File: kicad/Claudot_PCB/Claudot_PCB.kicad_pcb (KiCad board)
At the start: 2 copper layers, 104.8 x 57.2 mm, 51 parts, among them SW1 SW_Push, SW10 SW_Push, SW11 SW_Push, SW12 RotaryEncoder, SW2 SW_Push, SW3 SW_Push, SW4 SW_Push, SW5 SW_Push, SW6 SW_Push, SW7 SW_Push, SW8 SW_Push, SW9 SW_Push, U1 RP2040, U2 AP2112K-3.3, U3 W25Q16JVUXIQ, Y1 12MHz

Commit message: Update schematic and pcb
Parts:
- added R5: 27, Library:R_0402, F.Cu at (121.3, 88.2)
- added R6: 27, Library:R_0402, F.Cu at (122.3, 88.2)
- moved C4 3.58 mm to (124.3, 89.5), turned to 0 degrees
- moved C3 2.58 mm to (124.3, 90.5), turned to 0 degrees
- moved C10 1.05 mm to (124.3, 91.5)
- moved C6 0.60 mm to (113.8, 96.5)
- moved C8 0.60 mm to (124.3, 96.5)
- moved C11 0.25 mm to (120.3, 88.2)
- moved C12 0.25 mm to (119.3, 88.2)
- moved C14 0.25 mm to (118.3, 88.2)
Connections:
- U1 pad 46: unconnected-(U1-USB_DM-Pad46) -> D-
- U1 pad 47: unconnected-(U1-USB_DP-Pad47) -> D+
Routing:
- net GND: vias 10 -> 11
- net +1V1: vias 0 -> 2

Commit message: Update schematic and pcb
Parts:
- added J1: Conn_01x04, Connector_Molex:Molex_Pico-EZmate_78171-0004_1x04-1MP_P1.20mm_Vertical, F.Cu at (120.2, 82.5)
- added R3: 10K, Resistor_SMD:R_0402_1005Metric, F.Cu at (109.2, 88.3)
- added R4: 1K, Resistor_SMD:R_0402_1005Metric, F.Cu at (109.2, 89.3)
- moved C15 3.95 mm to (114.8, 83.0), turned to 180 degrees
- moved C16 3.51 mm to (114.8, 87.7), turned to 180 degrees
- moved C4 3.28 mm to (121.1, 90.0), turned to 90 degrees
- moved R6 3.02 mm to (119.8, 86.5)
- moved C3 2.27 mm to (122.1, 90.0), turned to 90 degrees
- moved U3 2.15 mm to (114.3, 85.3), turned to 180 degrees
- moved C10 1.88 mm to (123.1, 90.0), turned to 90 degrees
- moved R5 1.77 mm to (120.8, 86.5)
- moved C11 0.82 mm to (119.5, 88.4)
- moved C12 0.82 mm to (118.5, 88.4)
- moved C14 0.82 mm to (117.5, 88.4)
- moved U2 0.80 mm to (114.3, 89.5)
- renumbered U3 to U2, U2 to U3
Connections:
- net Net-(U1-QSPI_SS) renamed QSPI_SS_N
- net Net-(U1-RUN) renamed ~{RESET}
- C16 pad 1: Net-(U2-VOUT) -> +3V3
- R5 pad 1: D+ -> Net-(U1-USB_DM)
- R5 pad 2: unconnected-(R5-Pad2) -> D-
- R6 pad 1: D- -> Net-(U1-USB_DP)
- R6 pad 2: unconnected-(R6-Pad2) -> D+
- U1 pad 46: D- -> Net-(U1-USB_DM)
- U1 pad 47: D+ -> Net-(U1-USB_DP)
- U3 pad 5: Net-(U2-VOUT) -> +3V3
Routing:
- net GND: vias 11 -> 18
- net +3V3: vias 0 -> 4
- net +1V1: vias 2 -> 0

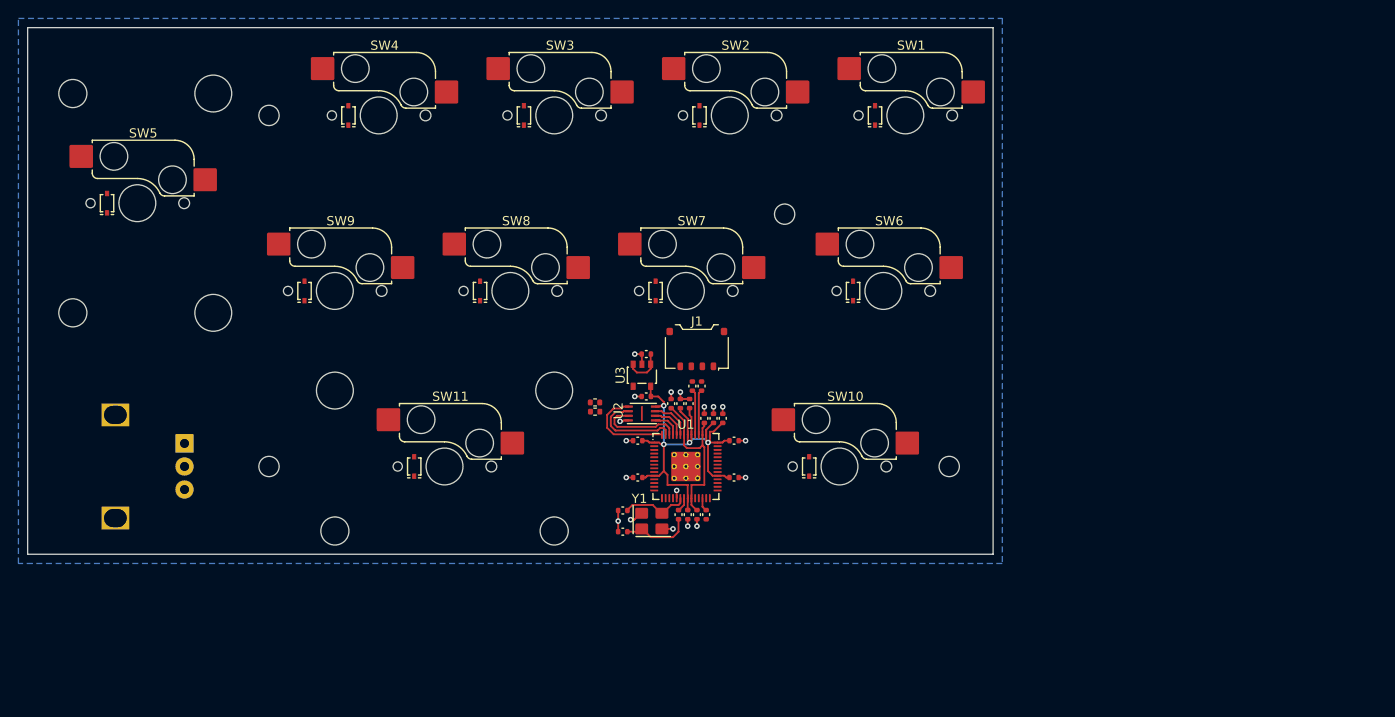
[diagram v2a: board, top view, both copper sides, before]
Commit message: Change J1 footprint
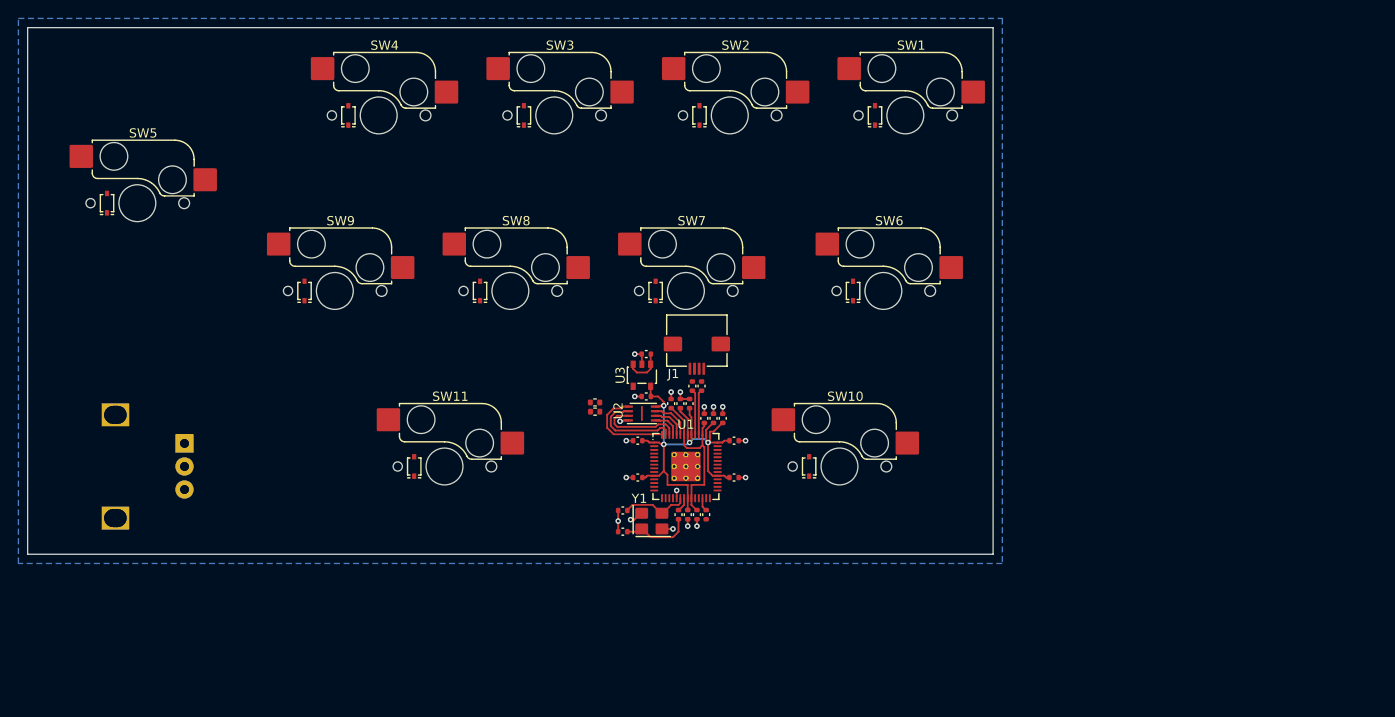
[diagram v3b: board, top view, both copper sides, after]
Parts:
- removed REF** (x2): MX_Switch_Stabilizer_2u, Library:MX_Switch_Stabilizer_2u
- removed REF** (x4): MountingHole_2.2mm_M2, MountingHole:MountingHole_2.2mm_M2
- J1: footprint Connector_Molex:Molex_Pico-EZmate_78171-0004_1x04-1MP_P1.20mm_Vertical -> Library:AFC01-S04FCC-00
- moved J1 0.80 mm to (120.2, 83.3)

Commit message: Update
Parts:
- added SW_B1: SKRP_Switch, Library:SKRP_Switch, F.Cu at (109.6, 114.1)
- added SW_R1: SKRP_Switch, Library:SKRP_Switch, F.Cu at (109.6, 118.7)
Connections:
- net QSPI_SS_N renamed QSPI_SS
- R4 pad 2: unconnected-(R4-Pad2) -> Net-(R4-Pad2)

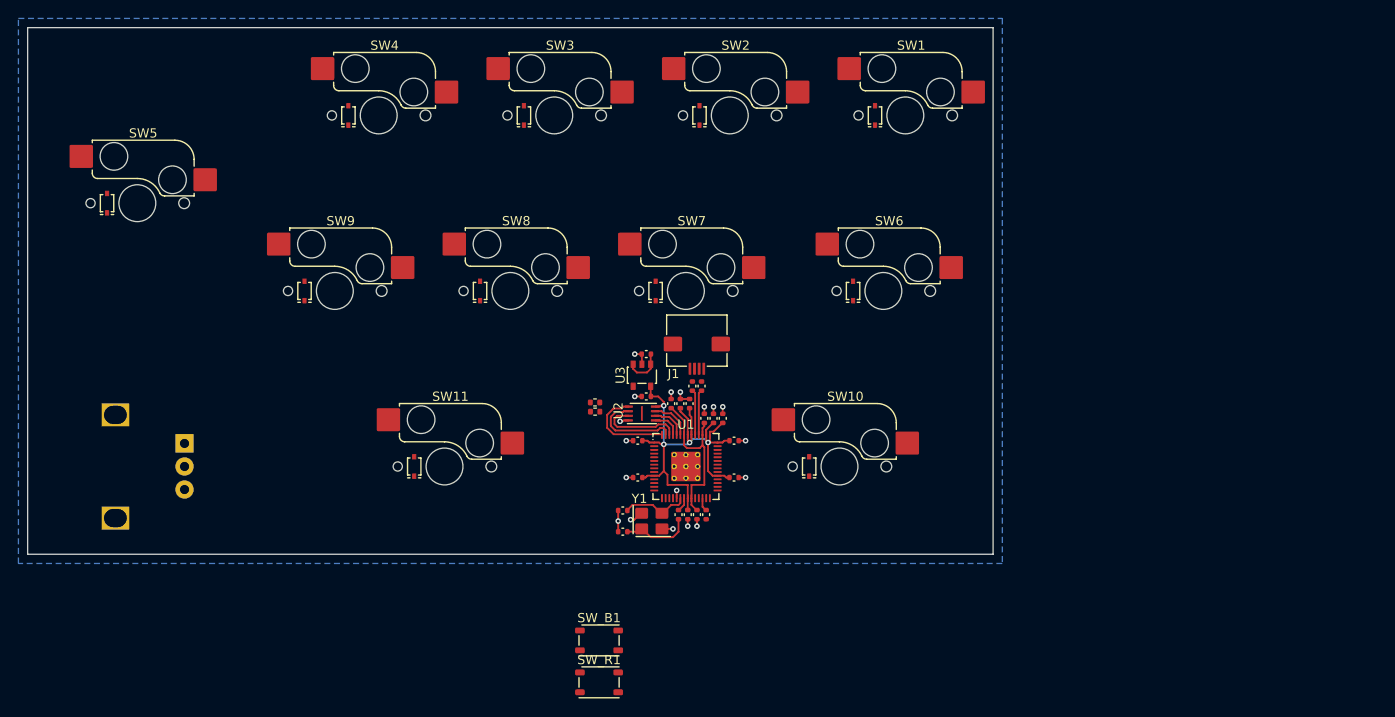
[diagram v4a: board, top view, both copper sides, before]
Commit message: Fix: restore missing hole
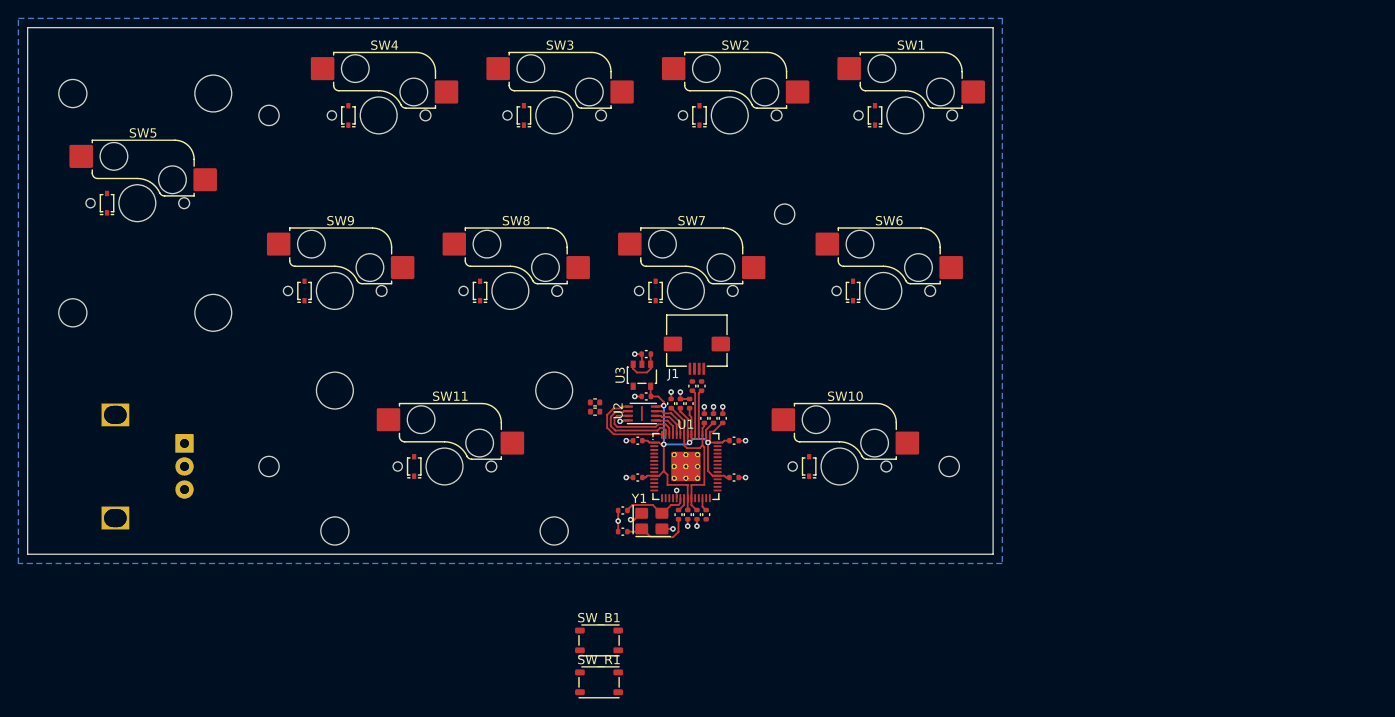
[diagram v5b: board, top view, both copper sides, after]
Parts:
- added REF**: MountingHole_2.2mm_M2, MountingHole:MountingHole_2.2mm_M2, B.Cu at (73.8, 95.2)
- added REF**: MountingHole_2.2mm_M2, MountingHole:MountingHole_2.2mm_M2, B.Cu at (129.8, 67.9)
- added REF**: MountingHole_2.2mm_M2, MountingHole:MountingHole_2.2mm_M2, B.Cu at (73.8, 57.1)
- added REF**: MX_Switch_Stabilizer_2u, Library:MX_Switch_Stabilizer_2u, B.Cu at (59.5, 66.7)
- added REF**: MountingHole_2.2mm_M2, MountingHole:MountingHole_2.2mm_M2, B.Cu at (147.6, 95.2)
- added REF**: MX_Switch_Stabilizer_2u, Library:MX_Switch_Stabilizer_2u, B.Cu at (92.9, 95.2)

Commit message: Update schematic and pcb
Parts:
- moved SW_R1 22.0 mm to (104.8, 97.2)
- moved SW_B1 21.4 mm to (104.8, 93.2)
- moved J1 0.09 mm to (120.3, 83.4)
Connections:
- R4 pad 1: QSPI_SS -> Net-(R4-Pad1)
- R4 pad 2: Net-(R4-Pad2) -> QSPI_SS
- SW_B1 pad 1: GND -> Net-(R4-Pad1)
- SW_B1 pad 2: (no net) -> Net-(R4-Pad1)
- SW_B1 pad 3: Net-(R4-Pad2) -> GND
- SW_B1 pad 4: (no net) -> GND
- SW_R1 pad 1: GND -> ~{RESET}
- SW_R1 pad 2: (no net) -> ~{RESET}
- SW_R1 pad 3: ~{RESET} -> GND
- SW_R1 pad 4: (no net) -> GND
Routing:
- net GND: vias 18 -> 19
- net +5V: vias 0 -> 2
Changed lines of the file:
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@@
 	(net 87 "~{RESET}")
 	(net 88 "QSPI_SS")
-	(net 89 "Net-(R4-Pad2)")
+	(net 89 "Net-(R4-Pad1)")
 	(footprint "Library:AFC01-S04FCC-00"
 		(layer "F.Cu")
-		(at 120.25 83.3 180)
+		(at 120.2625 83.385 180)
 		(tags "JUSHUO, FFC")
 		(property "Reference" "J1"
@@
 	(footprint "Library:SKRP_Switch"
 		(layer "F.Cu")
-		(at 109.6375 118.675)
+		(at 104.76875 97.25)
 		(tags "ALPSALPINE, SKRPABE010, C115360")
 		(property "Reference" "SW_R1"
@@
 		)
 		(property "Value" "SKRP_Switch"
-			(at 0 0 0)
+			(at 0 2.5 0)
 			(unlocked yes)
 			(layer "F.Fab")
+			(hide yes)
 			(effects
 				(font
-					(size 0.5 0.5)
-					(thickness 0.075)
+					(size 1 1)
+					(thickness 0.15)
 				)
 			)
@@
 		)
 		(fp_text user "${REFERENCE}"
-			(at 0 2.5 0)
+			(at 0 0 0)
 			(unlocked yes)
 			(layer "F.Fab")
 			(effects
 				(font
-					(size 1 1)
-					(thickness 0.15)
+					(size 0.5 0.5)
+					(thickness 0.075)
 				)
 			)
@@
 			(layers "F.Cu" "F.Mask" "F.Paste")
 			(roundrect_rratio 0.2307692308)
-			(net 46 "GND")
+			(net 87 "~{RESET}")
 			(pinfunction "1")
 			(pintype "passive")
@@
 			(layers "F.Cu" "F.Mask" "F.Paste")
 			(roundrect_rratio 0.2307692308)
+			(net 87 "~{RESET}")
+			(pinfunction "2")
+			(pintype "passive")
 			(thermal_bridge_angle 45)
 		)
@@
 			(layers "F.Cu" "F.Mask" "F.Paste")
 			(roundrect_rratio 0.2307692308)
-			(net 87 "~{RESET}")
+			(net 46 "GND")
 			(pinfunction "3")
 			(pintype "passive")
@@
 			(layers "F.Cu" "F.Mask" "F.Paste")
 			(roundrect_rratio 0.2307692308)
+			(net 46 "GND")
+			(pinfunction "4")
+			(pintype "passive")
 			(thermal_bridge_angle 45)
 		)
@@
 			(layers "F.Cu" "F.Mask" "F.Paste")
 			(roundrect_rratio 0.25)
-			(net 88 "QSPI_SS")
+			(net 89 "Net-(R4-Pad1)")
 			(pintype "passive")
 		)
@@
 			(layers "F.Cu" "F.Mask" "F.Paste")
 			(roundrect_rratio 0.25)
-			(net 89 "Net-(R4-Pad2)")
+			(net 88 "QSPI_SS")
 			(pintype "passive")
 		)
@@
 	(footprint "Library:SKRP_Switch"
 		(layer "F.Cu")
-		(at 109.6375 114.125)
+		(at 104.76875 93.25)
 		(tags "ALPSALPINE, SKRPABE010, C115360")
 		(property "Reference" "SW_B1"
@@
 		)
 		(property "Value" "SKRP_Switch"
-			(at 0 0 0)
+			(at 0 2.5 0)
 			(unlocked yes)
 			(layer "F.Fab")
+			(hide yes)
 			(effects
 				(font
-					(size 0.5 0.5)
-					(thickness 0.075)
+					(size 1 1)
+					(thickness 0.15)
 				)
 			)
@@
 		)
 		(fp_text user "${REFERENCE}"
-			(at 0 2.5 0)
+			(at 0 0 0)
 			(unlocked yes)
 			(layer "F.Fab")
 			(effects
 				(font
-					(size 1 1)
-					(thickness 0.15)
+					(size 0.5 0.5)
+					(thickness 0.075)
 				)
 			)
@@
 			(layers "F.Cu" "F.Mask" "F.Paste")
 			(roundrect_rratio 0.2307692308)
-			(net 46 "GND")
+			(net 89 "Net-(R4-Pad1)")
 			(pinfunction "1")
 			(pintype "passive")
@@
 			(layers "F.Cu" "F.Mask" "F.Paste")
 			(roundrect_rratio 0.2307692308)
+			(net 89 "Net-(R4-Pad1)")
+			(pinfunction "2")
+			(pintype "passive")
 			(thermal_bridge_angle 45)
 		)
@@
 			(layers "F.Cu" "F.Mask" "F.Paste")
 			(roundrect_rratio 0.2307692308)
-			(net 89 "Net-(R4-Pad2)")
+			(net 46 "GND")
 			(pinfunction "3")
 			(pintype "passive")
@@
 			(layers "F.Cu" "F.Mask" "F.Paste")
 			(roundrect_rratio 0.2307692308)
+			(net 46 "GND")
+			(pinfunction "4")
+			(pintype "passive")
 			(thermal_bridge_angle 45)
 		)
@@
 	)
 	(gr_line
+		(start 115.2375 83.05)
+		(end 115.9875 83.05)
+		(stroke
+			(width 0.2)
+			(type solid)
+		)
+		(layer "F.Cu")
+		(net 74)
+	)
+	(gr_line
 		(start 119.4625 92.65)
 		(end 119.6625 92.45)
@@
 	)
 	(gr_line
+		(start 120.7125 86.025)
+		(end 120.5125 85.825)
+		(stroke
+			(width 0.2)
+			(type solid)
+		)
+		(layer "F.Cu")
+		(net 83)
+	)
+	(gr_line
 		(start 117.6625 90.875)
 		(end 117.6625 91.8125)
@@
 	)
 	(gr_line
+		(start 120.0125 84.725)
+		(end 120.0125 85.825)
+		(stroke
+			(width 0.2)
+			(type solid)
+		)
+		(layer "F.Cu")
+		(net 76)
+	)
+	(gr_line
 		(start 116.2375 88.75)
 		(end 115.7125 88.75)
@@
 	)
 	(gr_line
+		(start 118.8625 85.125)
+		(end 119.5125 85.125)
+		(stroke
+			(width 0.2)
+			(type solid)
+		)
+		(layer "F.Cu")
+		(net 46)
+	)
+	(gr_line
 		(start 119.8125 87.025)
 		(end 120.0625 87.275)
@@
 	)
 	(gr_line
+		(start 120.5125 84.725)
+		(end 120.5125 85.825)
+		(stroke
+			(width 0.2)
+			(type solid)
+		)
+		(layer "F.Cu")
+		(net 83)
+	)
+	(gr_line
 		(start 115.2375 84.65)
 		(end 115.2375 84.15)
@@
 	)
 	(gr_line
+		(start 121.6625 85.125)
+		(end 121.0125 85.125)
+		(stroke
+			(width 0.2)
+			(type solid)
+		)
+		(layer "F.Cu")
+		(net 74)
+	)
+	(gr_line
 		(start 121.6625 92.45)
 		(end 121.6625 91.8125)
@@
 	)
 	(gr_line
+		(start 119.8125 86.025)
+		(end 120.0125 85.825)
+		(stroke
+			(width 0.2)
+			(type solid)
+		)
+		(layer "F.Cu")
+		(net 76)
+	)
+	(gr_line
 		(start 119.6625 92.45)
 		(end 119.6625 91.8125)
@@
 		(net 67)
 	)
+	(gr_line
+		(start 121.6625 83.05)
+		(end 121.6625 85.125)
+		(stroke
+			(width 0.2)
+			(type default)
+		)
+		(layer "B.Cu")
+		(net 74)
+	)
+	(gr_line
+		(start 115.9875 83.05)
+		(end 121.6625 83.05)
+		(stroke
+			(width 0.2)
+			(type default)
+		)
+		(layer "B.Cu")
+		(net 74)
+	)
 	(gr_rect
 		(start 91.0125 67.2)
@@
 	)
 	(via
+		(at 118.8625 85.125)
+		(size 0.6)
+		(drill 0.3)
+		(layers "F.Cu" "B.Cu")
+		(remove_unused_layers yes)
+		(keep_end_layers yes)
+		(zone_layer_connections)
+		(net 46)
+	)
+	(via
 		(at 125.5375 96.45)
 		(size 0.6)
@@
 		(net 67)
 	)
+	(via
+		(at 121.6625 85.125)
+		(size 0.6)
+		(drill 0.3)
+		(layers "F.Cu" "B.Cu")
+		(remove_unused_layers yes)
+		(keep_end_layers yes)
+		(zone_layer_connections)
+		(net 74)
+	)
+	(via
+		(at 115.9875 83.05)
+		(size 0.6)
+		(drill 0.3)
+		(layers "F.Cu" "B.Cu")
+		(remove_unused_layers yes)
+		(keep_end_layers yes)
+		(zone_layer_connections)
+		(net 74)
+	)
 	(zone
